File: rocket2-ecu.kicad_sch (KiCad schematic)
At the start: 25 parts, among them J1 ALARM, J2 SMA, P1 PAD_SMD, P2 PAD_SMD, P3 PAD_SMD, P4 PAD_SMD, Q1 DMG3402L

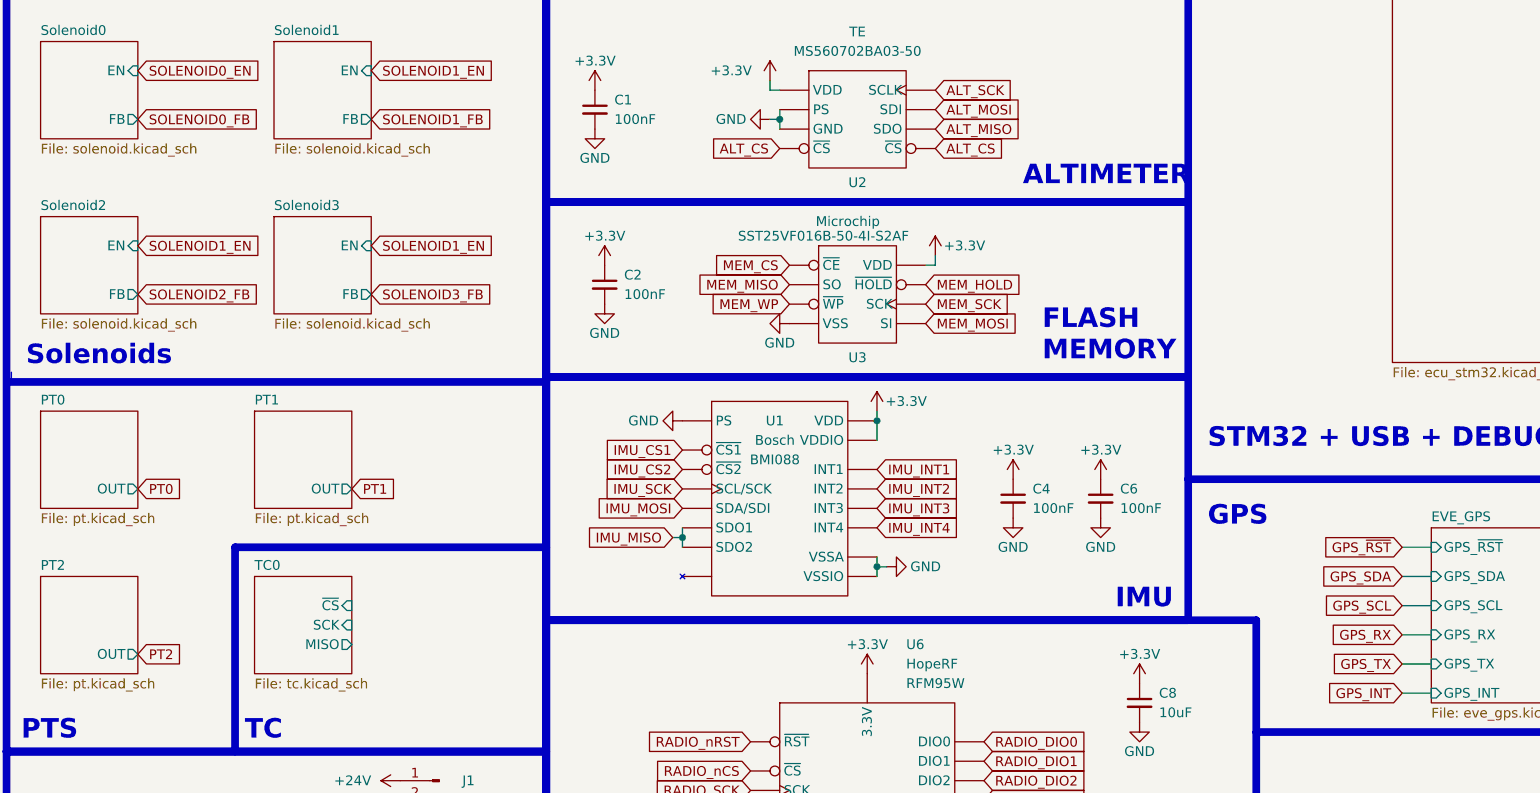
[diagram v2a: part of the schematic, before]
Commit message: added pin assignments to components on existing schematic
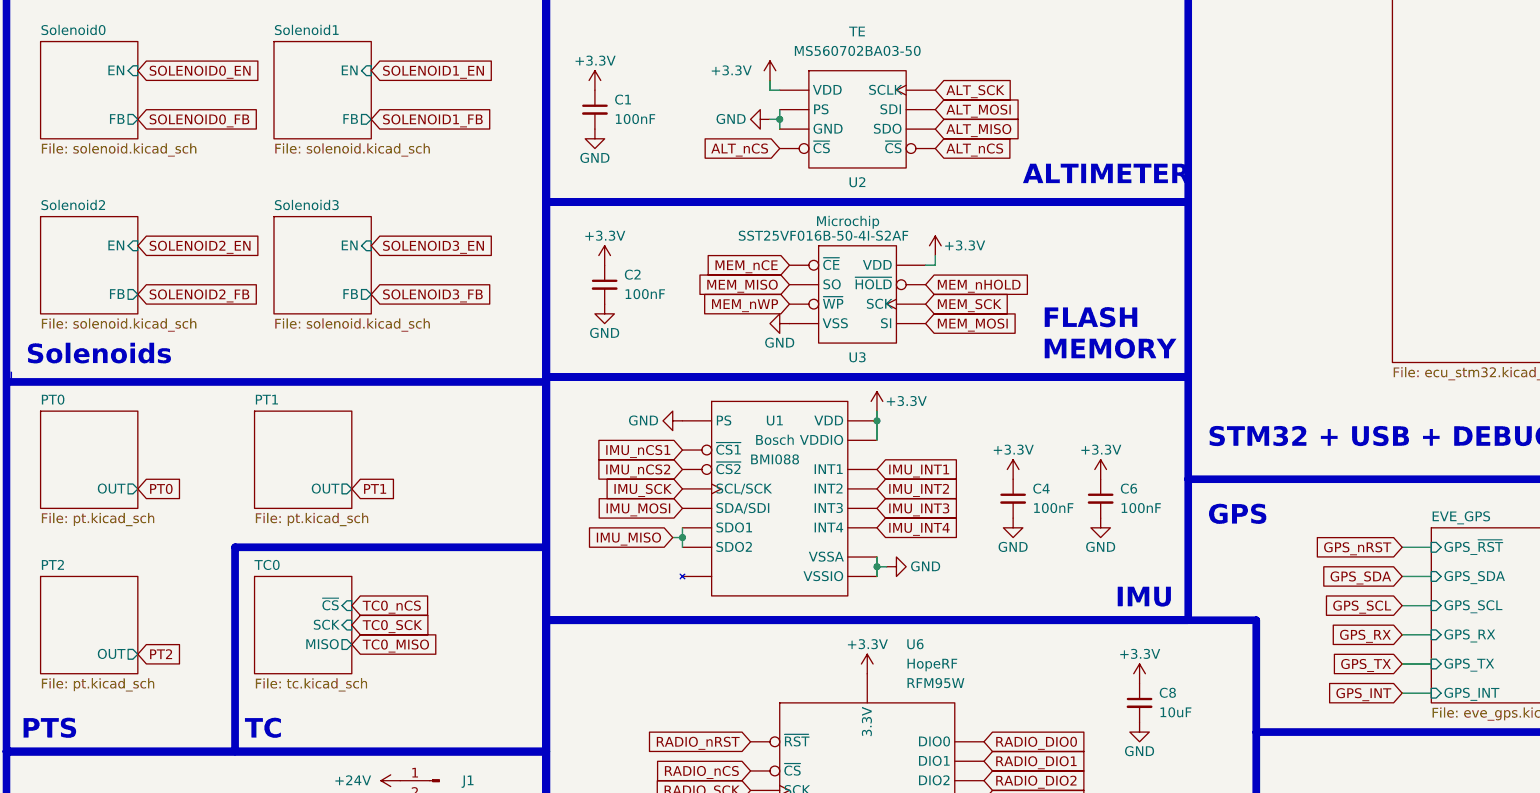
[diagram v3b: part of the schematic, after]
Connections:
- net ALT_CS renamed ALT_nCS
- net IMU_CS1 renamed IMU_nCS1
- net IMU_CS2 renamed IMU_nCS2
- net MEM_CS renamed MEM_nCE
- net MEM_HOLD renamed MEM_nHOLD
- net MEM_WP renamed MEM_nWP
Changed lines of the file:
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@@
     )
   )
-  (global_label "MEM_WP" (shape input) (at 114.3 109.22 180) (fields_autoplaced)
-    (effects (font (size 1.27 1.27)) (justify right))
-    (property "Intersheetrefs" "${INTERSHEET_REFS}" (at 103.574 109.22 0)
+  (global_label "MEM_nWP" (shape input) (at 114.3 109.22 180) (fields_autoplaced)
+    (effects (font (size 1.27 1.27)) (justify right))
+    (property "Intersheetrefs" "${INTERSHEET_REFS}" (at 102.5044 109.22 0)
       (effects (font (size 1.27 1.27)) (justify right) hide)
     )
@@
     )
   )
-  (global_label "SOLENOID1_EN" (shape input) (at 59.69 101.6 0) (fields_autoplaced)
+  (global_label "SOLENOID3_EN" (shape input) (at 59.69 101.6 0) (fields_autoplaced)
     (effects (font (size 1.27 1.27)) (justify left))
     (property "Intersheetrefs" "${INTERSHEET_REFS}" (at 76.5053 101.6 0)
@@
     )
   )
+  (global_label "TC0_SCK" (shape input) (at 57.15 151.13 0) (fields_autoplaced)
+    (effects (font (size 1.27 1.27)) (justify left))
+    (property "Intersheetrefs" "${INTERSHEET_REFS}" (at 68.22 151.13 0)
+      (effects (font (size 1.27 1.27)) (justify left) hide)
+    )
+  )
   (global_label "RADIO_DIO0" (shape input) (at 139.7 166.37 0) (fields_autoplaced)
     (effects (font (size 1.27 1.27)) (justify left))
@@
     )
   )
-  (global_label "ALT_CS" (shape input) (at 113.03 88.9 180) (fields_autoplaced)
-    (effects (font (size 1.27 1.27)) (justify right))
-    (property "Intersheetrefs" "${INTERSHEET_REFS}" (at 103.5134 88.9 0)
+  (global_label "ALT_nCS" (shape input) (at 113.03 88.9 180) (fields_autoplaced)
+    (effects (font (size 1.27 1.27)) (justify right))
+    (property "Intersheetrefs" "${INTERSHEET_REFS}" (at 102.4438 88.9 0)
       (effects (font (size 1.27 1.27)) (justify right) hide)
     )
@@
     )
   )
-  (global_label "IMU_CS2" (shape input) (at 100.33 130.81 180) (fields_autoplaced)
-    (effects (font (size 1.27 1.27)) (justify right))
-    (property "Intersheetrefs" "${INTERSHEET_REFS}" (at 89.3015 130.81 0)
-      (effects (font (size 1.27 1.27)) (justify right) hide)
-    )
-  )
-  (global_label "MEM_HOLD" (shape input) (at 132.08 106.68 0) (fields_autoplaced)
-    (effects (font (size 1.27 1.27)) (justify left))
-    (property "Intersheetrefs" "${INTERSHEET_REFS}" (at 145.0437 106.68 0)
+  (global_label "IMU_nCS2" (shape input) (at 100.33 130.81 180) (fields_autoplaced)
+    (effects (font (size 1.27 1.27)) (justify right))
+    (property "Intersheetrefs" "${INTERSHEET_REFS}" (at 88.2319 130.81 0)
+      (effects (font (size 1.27 1.27)) (justify right) hide)
+    )
+  )
+  (global_label "MEM_nHOLD" (shape input) (at 132.08 106.68 0) (fields_autoplaced)
+    (effects (font (size 1.27 1.27)) (justify left))
+    (property "Intersheetrefs" "${INTERSHEET_REFS}" (at 146.1133 106.68 0)
       (effects (font (size 1.27 1.27)) (justify left) hide)
     )
@@
     )
   )
-  (global_label "ALT_CS" (shape input) (at 133.35 88.9 0) (fields_autoplaced)
-    (effects (font (size 1.27 1.27)) (justify left))
-    (property "Intersheetrefs" "${INTERSHEET_REFS}" (at 142.8666 88.9 0)
+  (global_label "ALT_nCS" (shape input) (at 133.35 88.9 0) (fields_autoplaced)
+    (effects (font (size 1.27 1.27)) (justify left))
+    (property "Intersheetrefs" "${INTERSHEET_REFS}" (at 143.9362 88.9 0)
       (effects (font (size 1.27 1.27)) (justify left) hide)
     )
@@
     )
   )
-  (global_label "SOLENOID1_EN" (shape input) (at 29.21 101.6 0) (fields_autoplaced)
+  (global_label "SOLENOID2_EN" (shape input) (at 29.21 101.6 0) (fields_autoplaced)
     (effects (font (size 1.27 1.27)) (justify left))
     (property "Intersheetrefs" "${INTERSHEET_REFS}" (at 46.0253 101.6 0)
@@
     )
   )
-  (global_label "GPS_~{RST}" (shape input) (at 194.31 140.97 180) (fields_autoplaced)
-    (effects (font (size 1.27 1.27)) (justify right))
-    (property "Intersheetrefs" "${INTERSHEET_REFS}" (at 183.1606 140.97 0)
+  (global_label "GPS_nRST" (shape input) (at 194.31 140.97 180) (fields_autoplaced)
+    (effects (font (size 1.27 1.27)) (justify right))
+    (property "Intersheetrefs" "${INTERSHEET_REFS}" (at 182.091 140.97 0)
       (effects (font (size 1.27 1.27)) (justify right) hide)
     )
@@
     )
   )
-  (global_label "MEM_CS" (shape input) (at 114.3 104.14 180) (fields_autoplaced)
-    (effects (font (size 1.27 1.27)) (justify right))
-    (property "Intersheetrefs" "${INTERSHEET_REFS}" (at 103.8159 104.14 0)
-      (effects (font (size 1.27 1.27)) (justify right) hide)
+  (global_label "MEM_nCE" (shape input) (at 114.3 104.14 180) (fields_autoplaced)
+    (effects (font (size 1.27 1.27)) (justify right))
+    (property "Intersheetrefs" "${INTERSHEET_REFS}" (at 102.8068 104.14 0)
+      (effects (font (size 1.27 1.27)) (justify right) hide)
+    )
+  )
+  (global_label "TC0_MISO" (shape input) (at 57.15 153.67 0) (fields_autoplaced)
+    (effects (font (size 1.27 1.27)) (justify left))
+    (property "Intersheetrefs" "${INTERSHEET_REFS}" (at 69.0667 153.67 0)
+      (effects (font (size 1.27 1.27)) (justify left) hide)
     )
   )
@@
     )
   )
-  (global_label "IMU_CS1" (shape input) (at 100.33 128.27 180) (fields_autoplaced)
-    (effects (font (size 1.27 1.27)) (justify right))
-    (property "Intersheetrefs" "${INTERSHEET_REFS}" (at 89.3015 128.27 0)
+  (global_label "IMU_nCS1" (shape input) (at 100.33 128.27 180) (fields_autoplaced)
+    (effects (font (size 1.27 1.27)) (justify right))
+    (property "Intersheetrefs" "${INTERSHEET_REFS}" (at 88.2319 128.27 0)
       (effects (font (size 1.27 1.27)) (justify right) hide)
     )
@@
     )
   )
+  (global_label "TC0_nCS" (shape input) (at 57.15 148.59 0) (fields_autoplaced)
+    (effects (font (size 1.27 1.27)) (justify left))
+    (property "Intersheetrefs" "${INTERSHEET_REFS}" (at 68.099 148.59 0)
+      (effects (font (size 1.27 1.27)) (justify left) hide)
+    )
+  )

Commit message: Updated so only STM pins left really
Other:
- added sheet PT3 (pt.kicad_sch)
- added sheet PT4 (pt.kicad_sch)
- note added: "connect ALARM to a PWM enabled pin"
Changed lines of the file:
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@@
     (fill (type none))
+  )
+  (text_box "need to increase"
+    (at 147.32 97.79 0) (size 16.51 7.62)
+    (stroke (width 0) (type default))
+    (fill (type none))
+    (effects (font (size 1.27 1.27)) (justify left top))
+  )
+  (text "connect ALARM to a PWM enabled pin\n" (at 16.51 175.26 0)
+    (effects (font (size 1.27 1.27)) (justify left bottom))
   )
   (text "ALTIMETER" (at 144.78 93.98 0)
@@
     )
   )
+  (global_label "PT4" (shape input) (at 27.94 156.21 0) (fields_autoplaced)
+    (effects (font (size 1.27 1.27)) (justify left))
+    (property "Intersheetrefs" "${INTERSHEET_REFS}" (at 34.2929 156.21 0)
+      (effects (font (size 1.27 1.27)) (justify left) hide)
+    )
+  )
   (global_label "MEM_nWP" (shape input) (at 114.3 109.22 180) (fields_autoplaced)
     (effects (font (size 1.27 1.27)) (justify right))
@@
     )
   )
-  (global_label "PT0" (shape input) (at 29.21 133.35 0) (fields_autoplaced)
-    (effects (font (size 1.27 1.27)) (justify left))
-    (property "Intersheetrefs" "${INTERSHEET_REFS}" (at 35.6423 133.35 0)
+  (global_label "PT0" (shape input) (at 27.94 129.54 0) (fields_autoplaced)
+    (effects (font (size 1.27 1.27)) (justify left))
+    (property "Intersheetrefs" "${INTERSHEET_REFS}" (at 34.3723 129.54 0)
       (effects (font (size 1.27 1.27)) (justify left) hide)
     )
@@
     )
   )
-  (global_label "PT2" (shape input) (at 29.21 154.94 0) (fields_autoplaced)
-    (effects (font (size 1.27 1.27)) (justify left))
-    (property "Intersheetrefs" "${INTERSHEET_REFS}" (at 35.5629 154.94 0)
-      (effects (font (size 1.27 1.27)) (justify left) hide)
-    )
-  )
   (global_label "SOLENOID2_FB" (shape input) (at 29.21 107.95 0) (fields_autoplaced)
     (effects (font (size 1.27 1.27)) (justify left))
@@
     )
   )
+  (global_label "PT1" (shape input) (at 49.53 129.54 0) (fields_autoplaced)
+    (effects (font (size 1.27 1.27)) (justify left))
+    (property "Intersheetrefs" "${INTERSHEET_REFS}" (at 55.8829 129.54 0)
+      (effects (font (size 1.27 1.27)) (justify left) hide)
+    )
+  )
   (global_label "RADIO_DIO3" (shape input) (at 139.7 173.99 0) (fields_autoplaced)
     (effects (font (size 1.27 1.27)) (justify left))
@@
     )
   )
-  (global_label "PT1" (shape input) (at 57.15 133.35 0) (fields_autoplaced)
-    (effects (font (size 1.27 1.27)) (justify left))
-    (property "Intersheetrefs" "${INTERSHEET_REFS}" (at 63.5029 133.35 0)
+  (global_label "PT2" (shape input) (at 72.39 129.54 0) (fields_autoplaced)
+    (effects (font (size 1.27 1.27)) (justify left))
+    (property "Intersheetrefs" "${INTERSHEET_REFS}" (at 78.7429 129.54 0)
       (effects (font (size 1.27 1.27)) (justify left) hide)
     )
@@
     (effects (font (size 1.27 1.27)) (justify left))
     (property "Intersheetrefs" "${INTERSHEET_REFS}" (at 143.8341 109.22 0)
+      (effects (font (size 1.27 1.27)) (justify left) hide)
+    )
+  )
+  (global_label "PT3" (shape input) (at 27.94 143.51 0) (fields_autoplaced)
+    (effects (font (size 1.27 1.27)) (justify left))
+    (property "Intersheetrefs" "${INTERSHEET_REFS}" (at 34.2929 143.51 0)
       (effects (font (size 1.27 1.27)) (justify left) hide)
     )
@@
     )
   )
-  (sheet (at 16.51 144.78) (size 12.7 12.7) (fields_autoplaced)
+  (sheet (at 36.83 124.46) (size 12.7 6.35) (fields_autoplaced)
     (stroke (width 0.1524) (type solid))
     (fill (color 0 0 0 0.0000))
-    (property "Sheetname" "PT2" (at 16.51 144.0684 0)
+    (property "Sheetname" "PT1" (at 36.83 123.7484 0)
       (effects (font (size 1.27 1.27)) (justify left bottom))
     )
-    (property "Sheetfile" "pt.kicad_sch" (at 16.51 158.0646 0)
+    (property "Sheetfile" "pt.kicad_sch" (at 36.83 131.3946 0)
       (effects (font (size 1.27 1.27)) (justify left top))
     )
-    (pin "OUT" output (at 29.21 154.94 0)
+    (pin "OUT" output (at 49.53 129.54 0)
       (effects (font (size 1.27 1.27)) (justify right))
     )
@@
       )
       (project "rocket2-ecu"
-        (path "/02606b2c-b376-4ffb-9781-f9cea3f70994" (page "16"))
-      )
-    )
-  )
-  (sheet (at 44.45 123.19) (size 12.7 12.7) (fields_autoplaced)
+        (path "/02606b2c-b376-4ffb-9781-f9cea3f70994" (page "15"))
+      )
+    )
+  )
+  (sheet (at 15.24 151.13) (size 12.7 6.35) (fields_autoplaced)
     (stroke (width 0.1524) (type solid))
     (fill (color 0 0 0 0.0000))
-    (property "Sheetname" "PT1" (at 44.45 122.4784 0)
+    (property "Sheetname" "PT4" (at 15.24 150.4184 0)
       (effects (font (size 1.27 1.27)) (justify left bottom))
     )
-    (property "Sheetfile" "pt.kicad_sch" (at 44.45 136.4746 0)
+    (property "Sheetfile" "pt.kicad_sch" (at 15.24 158.0646 0)
       (effects (font (size 1.27 1.27)) (justify left top))
     )
-    (pin "OUT" output (at 57.15 133.35 0)
+    (pin "OUT" output (at 27.94 156.21 0)
       (effects (font (size 1.27 1.27)) (justify right))
     )
@@
       )
       (project "rocket2-ecu"
-        (path "/02606b2c-b376-4ffb-9781-f9cea3f70994" (page "15"))
+        (path "/02606b2c-b376-4ffb-9781-f9cea3f70994" (page "20"))
       )
     )
@@
     )
   )
+  (sheet (at 59.69 124.46) (size 12.7 6.35) (fields_autoplaced)
+    (stroke (width 0.1524) (type solid))
+    (fill (color 0 0 0 0.0000))
+    (property "Sheetname" "PT2" (at 59.69 123.7484 0)
+      (effects (font (size 1.27 1.27)) (justify left bottom))
+    )
+    (property "Sheetfile" "pt.kicad_sch" (at 59.69 131.3946 0)
+      (effects (font (size 1.27 1.27)) (justify left top))
+    )
+    (pin "OUT" output (at 72.39 129.54 0)
+      (effects (font (size 1.27 1.27)) (justify right))
+    )
+    (instances
+      (project "rocket2-gse"
+        (path "/94c3ca0c-6aa1-4bff-ab47-a0279d059895" (page "13"))
+      )
+      (project "rocket2-ecu"
+        (path "/02606b2c-b376-4ffb-9781-f9cea3f70994" (page "16"))
+      )
+    )
+  )
   (sheet (at 16.51 97.79) (size 12.7 12.7) (fields_autoplaced)
     (stroke (width 0.1524) (type solid))
@@
     )
   )
-  (sheet (at 16.51 123.19) (size 12.7 12.7) (fields_autoplaced)
+  (sheet (at 15.24 124.46) (size 12.7 6.35) (fields_autoplaced)
     (stroke (width 0.1524) (type solid))
     (fill (color 0 0 0 0.0000))
-    (property "Sheetname" "PT0" (at 16.51 122.4784 0)
+    (property "Sheetname" "PT0" (at 15.24 123.7484 0)
       (effects (font (size 1.27 1.27)) (justify left bottom))
     )
-    (property "Sheetfile" "pt.kicad_sch" (at 16.51 136.4746 0)
+    (property "Sheetfile" "pt.kicad_sch" (at 15.24 131.3946 0)
       (effects (font (size 1.27 1.27)) (justify left top))
     )
-    (pin "OUT" output (at 29.21 133.35 0)
+    (pin "OUT" output (at 27.94 129.54 0)
       (effects (font (size 1.27 1.27)) (justify right))
     )
@@
       )
     )
+  )
+  (sheet (at 15.24 138.43) (size 12.7 6.35) (fields_autoplaced)
+    (stroke (width 0.1524) (type solid))
+    (fill (color 0 0 0 0.0000))
+    (property "Sheetname" "PT3" (at 15.24 137.7184 0)
+      (effects (font (size 1.27 1.27)) (justify left bottom))
+    )
+    (property "Sheetfile" "pt.kicad_sch" (at 15.24 145.3646 0)
+      (effects (font (size 1.27 1.27)) (justify left top))
+    )
+    (pin "OUT" output (at 27.94 143.51 0)
+      (effects (font (size 1.27 1.27)) (justify right))
+    )
+    (instances
+      (project "rocket2-gse"
+        (path "/94c3ca0c-6aa1-4bff-ab47-a0279d059895" (page "13"))
+      )
+      (project "rocket2-ecu"
+        (path "/02606b2c-b376-4ffb-9781-f9cea3f70994" (page "17"))
+      )
+    )

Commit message: added capacitors and resolved all comments
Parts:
- U3: Manufacturer Microchip -> Renesas Electronics Corporation; Part # SST25VF016B-50-4I-S2AF -> AT25SL128A-MHE-T

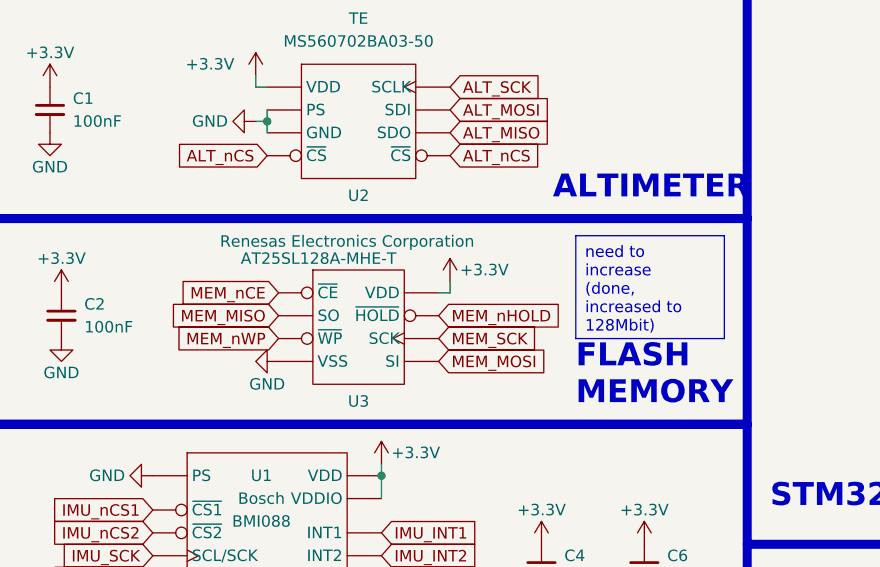
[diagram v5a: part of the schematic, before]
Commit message: added flash memory and ldos
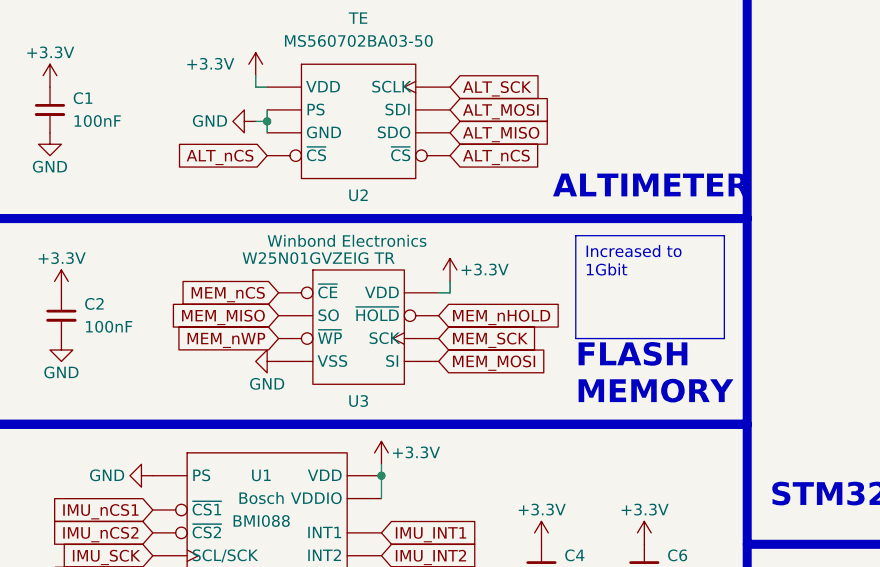
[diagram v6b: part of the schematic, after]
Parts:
- U3: Manufacturer Renesas Electronics Corporation -> Winbond Electronics; Part # AT25SL128A-MHE-T -> W25N01GVZEIG TR
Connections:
- net MEM_nCE renamed MEM_nCS
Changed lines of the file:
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@@
 		)
 	)
-	(text_box "need to increase (done, increased to 128Mbit)"
+	(text_box "Increased to 1Gbit"
 		(exclude_from_sim no)
 		(at 147.32 97.79 0)
@@
 		)
 	)
-	(global_label "MEM_nCE"
+	(global_label "MEM_nCS"
 		(shape input)
 		(at 114.3 104.14 180)
@@
 		)
 		(property "Intersheetrefs" "${INTERSHEET_REFS}"
-			(at 102.8068 104.14 0)
+			(at 102.6669 104.14 0)
 			(effects
 				(font
@@
 			)
 		)
-		(property "Datasheet" "https://www.renesas.com/us/en/document/dst/at25sl128a-datasheet?r=1608821"
+		(property "Datasheet" "https://www.winbond.com/resource-files/w25n01gv%20revl%20050918%20unsecured.pdf"
 			(at 122.936 107.95 0)
 			(effects
@@
 			)
 		)
-		(property "Manufacturer" "Renesas Electronics Corporation"
+		(property "Manufacturer" "Winbond Electronics"
 			(at 121.92 98.425 0)
 			(effects
@@
 			)
 		)
-		(property "Part #" "AT25SL128A-MHE-T"
+		(property "Part #" "W25N01GVZEIG TR"
 			(at 118.745 100.33 0)
 			(effects
